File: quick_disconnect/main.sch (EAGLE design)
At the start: 12 parts

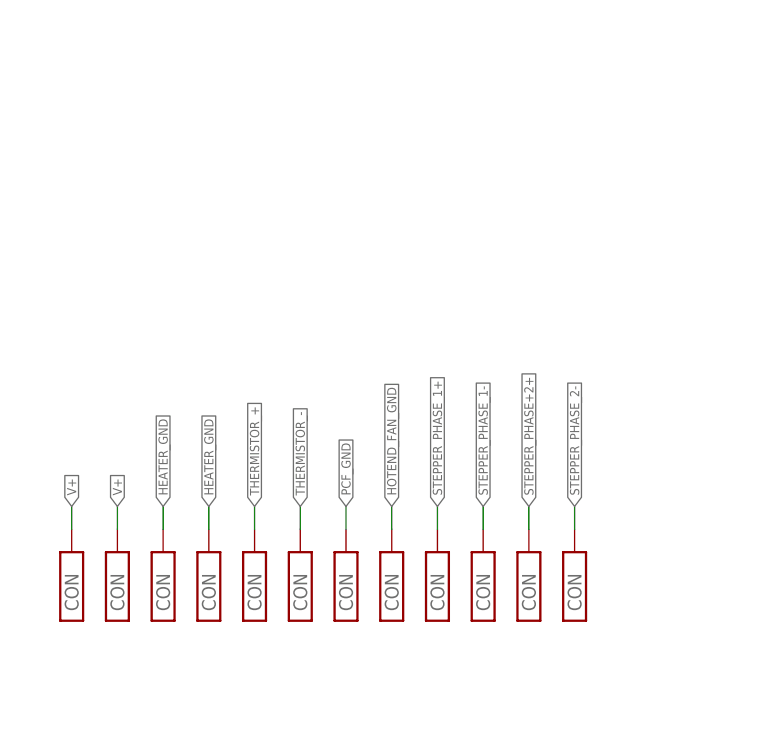
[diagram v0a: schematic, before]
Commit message: initial design of 4x 2pin molex, 1x 16 pin molex, 4 header acc
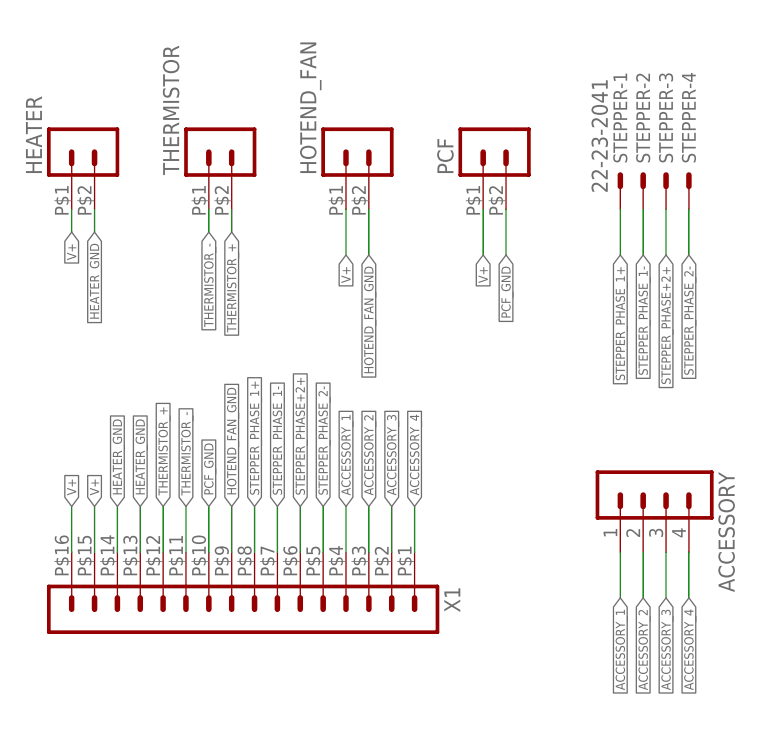
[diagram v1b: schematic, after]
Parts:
- removed U$1, U$10, U$11, U$12, U$2, U$3, U$4, U$5, U$6, U$7, U$8, U$9: PRECI-DIP_90022-AS, eric_personal_parts:PRECI-DIP_90022-AS
- added ACCESSORY: (no value), con-lstb:MA04-1
- added HEATER, HOTEND_FAN, PCF, THERMISTOR: (no value), con-molex-micro-fit-3_0:HEADER_POS2_43650-0224
- added STEPPER: 22-23-2041, con-molex:22-23-2041
- added X1: (no value), con-molex-micro-fit-3_0:HEADER_POS16_43045-1618
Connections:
- new net ACCESSORY_1: ACCESSORY.1, X1.4
- new net ACCESSORY_2: ACCESSORY.2, X1.3
- new net ACCESSORY_3: ACCESSORY.3, X1.2
- new net ACCESSORY_4: ACCESSORY.4, X1.1
- net HEATER_GND: now also HEATER.2, X1.13, X1.14; no longer U$3.CON, U$4.CON
- net HOTEND_FAN_GND: now also HOTEND_FAN.2, X1.9; no longer U$8.CON
- net PCF_GND: now also PCF.2, X1.10; no longer U$7.CON
- net STEPPER_PHASE+2+: now also STEPPER-3.S, X1.6; no longer U$12.CON
- net STEPPER_PHASE_1+: now also STEPPER-1.S, X1.8; no longer U$9.CON
- net STEPPER_PHASE_1-: now also STEPPER-2.S, X1.7; no longer U$10.CON
- net STEPPER_PHASE_2-: now also STEPPER-4.S, X1.5; no longer U$11.CON
- net THERMISTOR_+: now also THERMISTOR.2, X1.12; no longer U$5.CON
- net THERMISTOR_-: now also THERMISTOR.1, X1.11; no longer U$6.CON
- net V+: now also HEATER.1, HOTEND_FAN.1, PCF.1, X1.15, X1.16; no longer U$1.CON, U$2.CON
